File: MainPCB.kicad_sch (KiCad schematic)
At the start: 70 parts, among them IC1 VNH7070ASTR, IC2 VNH7070ASTR, IC3 VNH7070ASTR, IC4 VNH7070ASTR, J1 Conn_01x06, J10 Conn_01x02, J11 Conn_01x03, J12 Conn_01x04, J2 RaspberryPi, J3 Conn_01x02, J4 Conn_01x02, J5 Screw_Terminal_01x02, J6 Conn_02x05_Odd_Even, J7 Conn_01x03, J8 Conn_01x02, J9 Conn_01x02, M1 Motor_DC, M2 Motor_DC, M3 Motor_DC, M4 Motor_DC, SW1 SW_DPST_x2, SW2 SW_SPDT, SW3 SW_SPDT, SW4 SW_SPDT, SW5 SW_SPDT, U1 V_Regulator3.3v, U10 N channel, U12 Teensy4.1, U2 V_Regulator5v, U4 V_Regulator5v, U5 Compass

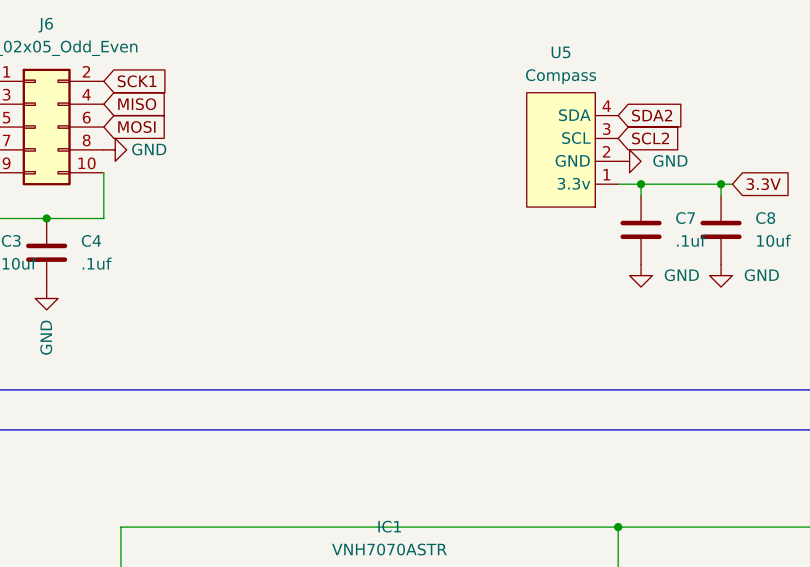
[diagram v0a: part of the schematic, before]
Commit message: Fixed Holes error
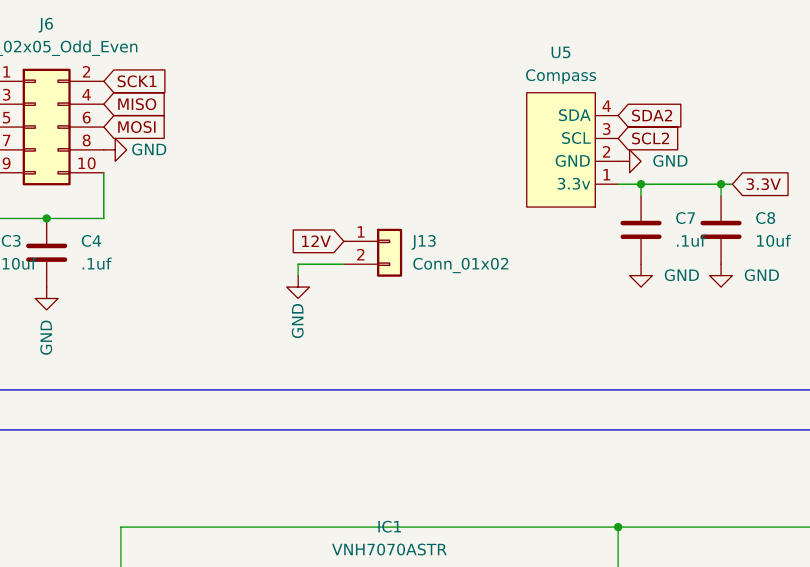
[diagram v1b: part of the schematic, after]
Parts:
- added J13: Conn_01x02, Connector_JST:JST_XH_B2B-XH-A_1x02_P2.50mm_Vertical, symbol Connector_Generic:Conn_01x02
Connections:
- net 12V: now also J13.1 (Pin_1)
- net GND: now also J13.2 (Pin_2)
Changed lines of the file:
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@@
 	(wire
 		(pts
+			(xy 100.33 266.7) (xy 100.33 267.97)
+		)
+		(stroke
+			(width 0)
+			(type default)
+		)
+	)
+	(wire
+		(pts
 			(xy 80.645 355.6) (xy 80.645 365.125)
 		)
@@
 	(wire
 		(pts
+			(xy 105.41 266.7) (xy 100.33 266.7)
+		)
+		(stroke
+			(width 0)
+			(type default)
+		)
+	)
+	(wire
+		(pts
 			(xy 129.54 27.94) (xy 128.27 27.94)
 		)
@@
 		)
 	)
+	(global_label "12V"
+		(shape input)
+		(at 105.41 264.16 180)
+		(fields_autoplaced yes)
+		(effects
+			(font
+				(size 1.27 1.27)
+			)
+			(justify right)
+		)
+		(property "Intersheetrefs" "${INTERSHEET_REFS}"
+			(at 98.9172 264.16 0)
+			(effects
+				(font
+					(size 1.27 1.27)
+				)
+				(justify right)
+				(hide yes)
+			)
+		)
+	)
 	(global_label "SCK1"
 		(shape input)
@@
 	(symbol
 		(lib_id "power:GND")
+		(at 100.33 267.97 0)
+		(unit 1)
+		(exclude_from_sim no)
+		(in_bom yes)
+		(on_board yes)
+		(dnp no)
+		(property "Reference" "#PWR017"
+			(at 100.33 274.32 0)
+			(effects
+				(font
+					(size 1.27 1.27)
+				)
+				(hide yes)
+			)
+		)
+		(property "Value" "GND"
+			(at 100.33 271.018 90)
+			(effects
+				(font
+					(size 1.27 1.27)
+				)
+				(justify right)
+			)
+		)
+		(property "Footprint" ""
+			(at 100.33 267.97 0)
+			(effects
+				(font
+					(size 1.27 1.27)
+				)
+				(hide yes)
+			)
+		)
+		(property "Datasheet" ""
+			(at 100.33 267.97 0)
+			(effects
+				(font
+					(size 1.27 1.27)
+				)
+				(hide yes)
+			)
+		)
+		(property "Description" ""
+			(at 100.33 267.97 0)
+			(effects
+				(font
+					(size 1.27 1.27)
+				)
+				(hide yes)
+			)
+		)
+		(pin "1"
+		)
+		(instances
+			(project "MainPCB"
+				(path "/ffac2233-fa42-49ac-90d7-860e528f7ebd"
+					(reference "#PWR017")
+					(unit 1)
+				)
+			)
+		)
+	)
+	(symbol
+		(lib_id "power:GND")
 		(at 128.27 39.37 0)
 		(unit 1)
@@
 					(unit 1)
 				)
+			)
+		)
+	)
+	(symbol
+		(lib_id "Connector_Generic:Conn_01x02")
+		(at 110.49 264.16 0)
+		(unit 1)
+		(exclude_from_sim no)
+		(in_bom yes)
+		(on_board yes)
+		(dnp no)
+		(fields_autoplaced yes)
+		(property "Reference" "J13"
+			(at 113.03 264.1599 0)
+			(effects
+				(font
+					(size 1.27 1.27)
+				)
+				(justify left)
+			)
+		)
+		(property "Value" "Conn_01x02"
+			(at 113.03 266.6999 0)
+			(effects
+				(font
+					(size 1.27 1.27)
+				)
+				(justify left)
+			)
+		)
+		(property "Footprint" "Connector_JST:JST_XH_B2B-XH-A_1x02_P2.50mm_Vertical"
+			(at 110.49 264.16 0)
+			(effects
+				(font
+					(size 1.27 1.27)
+				)
+				(hide yes)
+			)
+		)
+		(property "Datasheet" "~"
+			(at 110.49 264.16 0)
+			(effects
+				(font
+					(size 1.27 1.27)
+				)
+				(hide yes)
+			)
+		)
+		(property "Description" "Generic connector, single row, 01x02, script generated (kicad-library-utils/schlib/autogen/connector/)"
+			(at 110.49 264.16 0)
+			(effects
+				(font
+					(size 1.27 1.27)
+				)
+				(hide yes)
+			)
+		)
+		(pin "2"
+		)
+		(pin "1"
+		)
+		(instances
+			(project "MainPCB"
+				(path "/ffac2233-fa42-49ac-90d7-860e528f7ebd"
+					(reference "J13")
+					(unit 1)
+				)

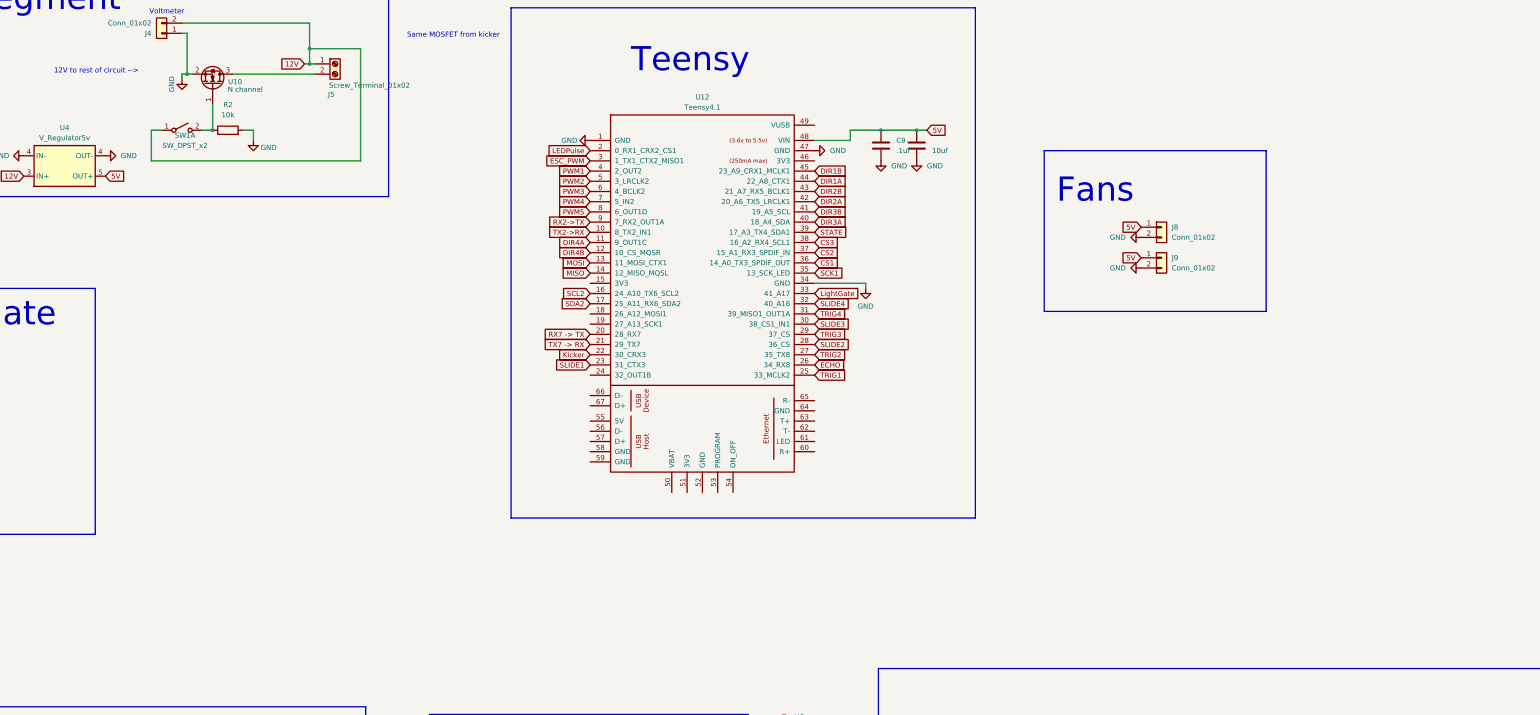
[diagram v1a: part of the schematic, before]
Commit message: Added Boost Converter
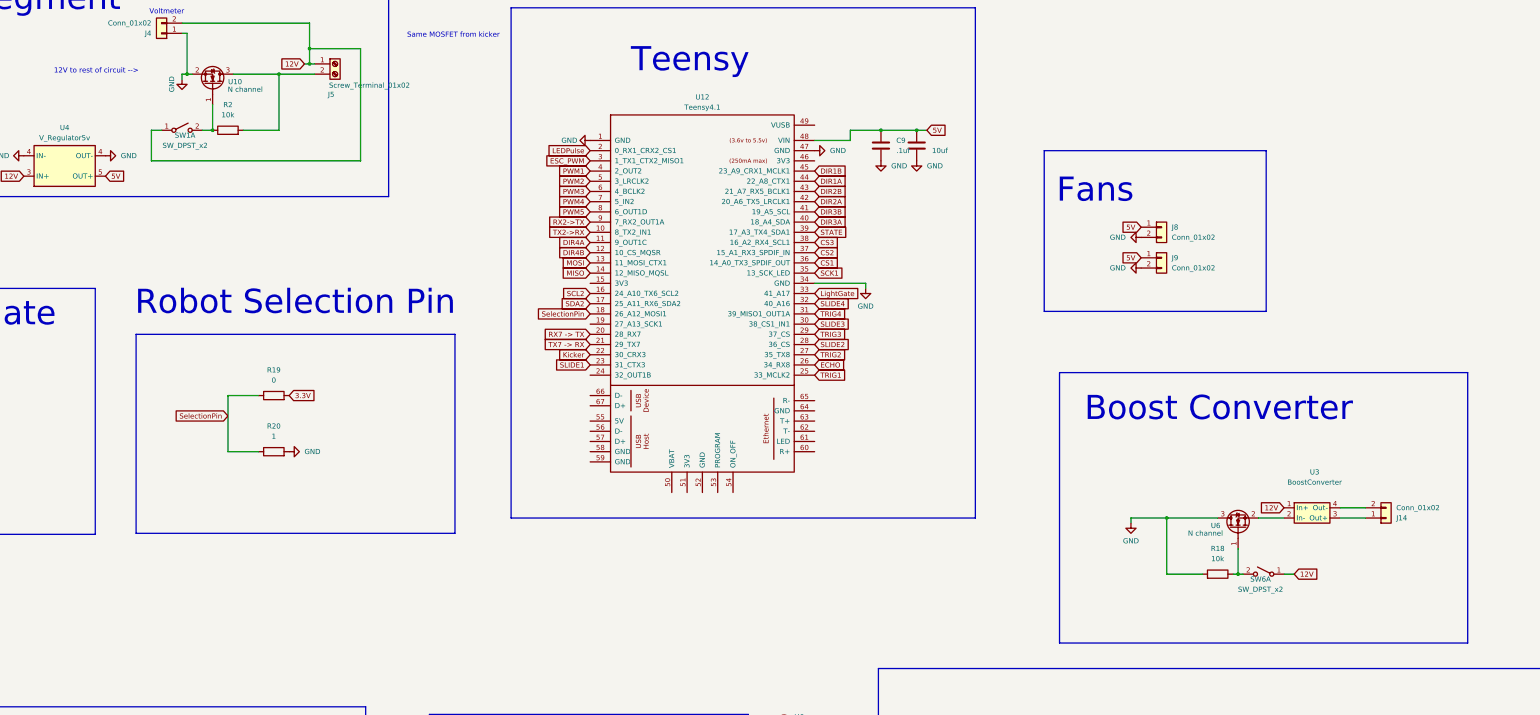
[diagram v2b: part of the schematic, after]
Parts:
- added J14: Conn_01x02, Connector_JST:JST_XH_B2B-XH-A_1x02_P2.50mm_Vertical, symbol Connector_Generic:Conn_01x02
- added R18: 10k, Capacitor_SMD:C_0805_2012Metric_Pad1.18x1.45mm_HandSolder, symbol Device:R
- added R19: 0, Resistor_SMD:R_0805_2012Metric_Pad1.20x1.40mm_HandSolder, symbol Device:R
- added R20: 1, Resistor_SMD:R_0805_2012Metric_Pad1.20x1.40mm_HandSolder, symbol Device:R
- added SW6: SW_DPST_x2, SlideSW:SPDT_OS102011_CNK, symbol Switch:SW_DPST_x2
- added U3: BoostConverter, BoostConverter:Boost_Convertor_LM2577, symbol BoostConverter:BoostConverter
- added U6: N channel, Package_TO_SOT_THT:TO-220-3_Vertical, symbol Transistor_FET:2N7002K
- SW1: footprint ToggleSwitch:ANT11SECQE -> SlideSW:SPDT_OS102011_CNK
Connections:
- net 12V: now also SW6.1 (A), U3.1 (In+)
- net 3.3V: now also R19.2
- net GND: now also R18.2, R20.2, U6.3 (D); no longer R2.2
- net at J5.2 (Pin_2), U10.3 (D): now also R2.2
- net SelectionPin: now reaches U12.18 (26_A12_MOSI1)
- net SelectionPin: now also R19.1, R20.1
- new net: R18.1, SW6.2 (B), U6.1 (G)
- new net: U3.2 (In-), U6.2 (S)
- new net: J14.1 (Pin_1), U3.3 (Out+)
- new net: J14.2 (Pin_2), U3.4 (Out-)
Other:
- note added: "Boost Converter"
- note added: "Robot Selection Pin"

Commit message: changed a lot
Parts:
- removed J12: Conn_01x04, Connector_PinHeader_2.54mm:PinHeader_1x04_P2.54mm_Vertical, symbol Connector_Generic:Conn_01x04
- removed J13: Conn_01x02, Connector_JST:JST_XH_B2B-XH-A_1x02_P2.50mm_Vertical, symbol Connector_Generic:Conn_01x02
- removed J3: Conn_01x02, Connector_PinHeader_2.54mm:PinHeader_2x01_P2.54mm_Vertical, symbol Connector_Generic:Conn_01x02
- removed J7: Conn_01x03, Connector_PinHeader_2.54mm:PinHeader_1x03_P2.54mm_Vertical, symbol Connector_Generic:Conn_01x03
- removed U5: Compass, Custom:Compass Sensor DFRobot, symbol Compass_Sensor:SEN0140
- added C15: 0.1uf, Capacitor_SMD:C_0805_2012Metric_Pad1.18x1.45mm_HandSolder, symbol Device:C
- added IC5: VNH7070ASTR, VNH:SOIC127P600X175-16N, symbol VNH7070ASTR:VNH7070ASTR
- added J13: Conn_01x03, Connector_PinHeader_2.54mm:PinHeader_1x03_P2.54mm_Vertical, symbol Connector_Generic:Conn_01x03
- added J15, J16: Conn_01x05, Connector_JST:JST_XH_B5B-XH-A_1x05_P2.50mm_Vertical, symbol Connector_Generic:Conn_01x05
- added M5: Motor_DC, Connector_JST:JST_XH_B2B-XH-AM_1x02_P2.50mm_Vertical, symbol Motor:Motor_DC
- added R21: 10k, Capacitor_SMD:C_0805_2012Metric, symbol Device:R
- added R22: 15k, Capacitor_SMD:C_0805_2012Metric, symbol Device:R
- added R23, R24, R25: 100, Resistor_SMD:R_0805_2012Metric_Pad1.20x1.40mm_HandSolder, symbol Device:R
- added U7: 4554, 4554:MODULE_4554, symbol 4554:4554
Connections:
- net 12V: now also IC5.12 (VCC_3), IC5.4 (VCC_1), IC5.5 (VCC_2)
- net 3.3V: now also J13.1 (Pin_1), R23.1, U7.JP1_1 (VIN)
- net 5V: now also J15.1 (Pin_1), J16.1 (Pin_1)
- net ECHO: now also R21.1, R22.2
- net GND: now also IC5.1 (GND_A_1), IC5.16 (GND_A_2), IC5.8 (GND_B_1), IC5.9 (GND_B_2), J13.2 (Pin_2), J15.2 (Pin_2), J16.2 (Pin_2), R22.1, R24.1, U7.JP1_3 (GND_JP1)
- net PWM5: now also R25.2
- net SCL2: now also U7.JP1_4 (SCK/SCL)
- net SDA2: now also U7.JP1_5 (SDI/SDA)
- net SLIDE1: now also J13.3 (Pin_3)
- net TRIG1: now also J16.3 (Pin_3)
- net TRIG2: now also J16.4 (Pin_4)
- net TRIG3: now also J15.3 (Pin_3)
- net TRIG4: now also J15.4 (Pin_4)
- new net: J15.5 (Pin_5), J16.5 (Pin_5), R21.2
- new net: IC5.11 (PWM), R25.1
- new net: C15.2, IC5.10 (OUT_B_2), IC5.7 (OUT_B_1), M5.2 (-)
- new net: C15.1, IC5.15 (OUT_A_2), IC5.2 (OUT_A_1), M5.1 (+)
- new net: IC5.3 (IN_A), R23.2
- new net: IC5.6 (IN_B), R24.2
- no-connect marks 8 -> 10
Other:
- note added: "Comm Module"
- note added: "Ultrasonics"
- note removed: "Electronic Speed Controller"
- note removed: "For Level Shifter (If needed)"
- moved on the sheet: C7, C8
